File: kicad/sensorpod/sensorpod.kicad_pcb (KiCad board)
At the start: 2 copper layers, 55.4 x 79.5 mm, 48 parts, among them M1 MOTOR, P1 HEADER_(8_WAY), Q1 IRFML8244TRPBF

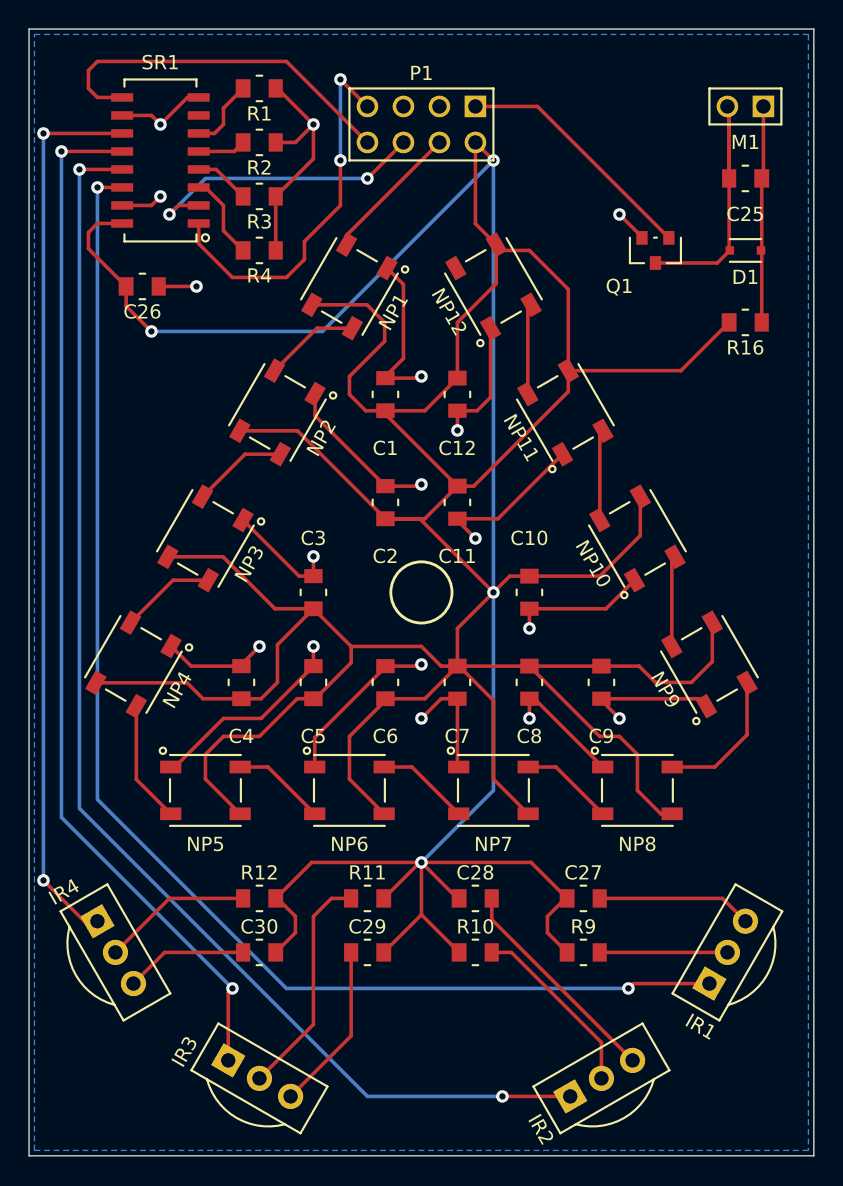
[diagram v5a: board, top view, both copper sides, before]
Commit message: Updated sensorpod schematic and PCB to fit into Serpac C9 enclosure
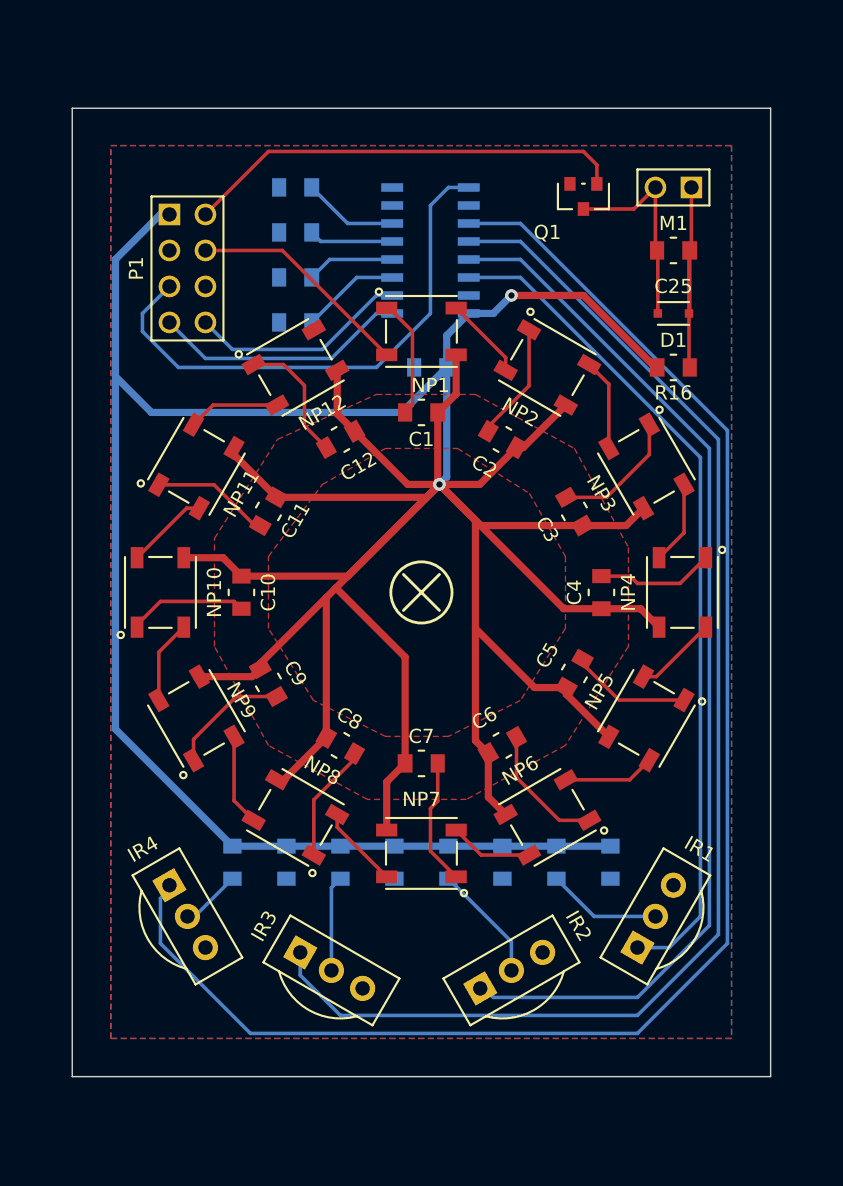
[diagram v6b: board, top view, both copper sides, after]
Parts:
- C26, C27, C28, C29, C30, R1, R10, R11, R12, R2, R3, R4, R9, SR1: moved to B.Cu
- moved NP4 39.1 mm to (216.5, 176.5), turned to 90 degrees
- moved NP9 36.4 mm to (182.2, 185.4)
- moved NP10 33.9 mm to (179.7, 176.5), turned to 270 degrees
- moved NP3 31.5 mm to (214.0, 167.6), turned to 120 degrees
- moved NP5 31.5 mm to (214.0, 185.4), turned to 60 degrees
- moved NP11 26.3 mm to (182.2, 167.6), turned to 240 degrees
- moved C4 26.2 mm to (210.8, 176.5)
- moved C30 25.6 mm to (211.5, 195.6), turned to 270 degrees
- moved NP8 24.2 mm to (189.2, 192.4), turned to 330 degrees
- moved C9 23.5 mm to (187.3, 182.9), turned to 300 degrees
- moved C27 21.1 mm to (188.6, 195.6), turned to 270 degrees
- moved C26 21.1 mm to (198.8, 160.7), turned to 180 degrees
- moved C10 20.3 mm to (185.4, 176.5)
- moved SR1 20.1 mm to (198.8, 152.4)
- moved P1 19.4 mm to (181.6, 153.7), turned to 270 degrees
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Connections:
- P1 pad 1: N-0000020 (its old number) -> +5V
- P1 pad 2: +5V -> N-0000021
- P1 pad 5: GND -> N-0000022
- P1 pad 6: N-0000018 (its old number) -> GND
- P1 pad 8: N-0000022 -> N-0000023
- Q1 pad 1: N-0000020 (its old number) -> N-0000021
- SR1 pad 2: N-0000018 (its old number) -> N-0000023
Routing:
- net GND: track 198.4 -> 104.0 mm, vias 17 -> 0
- net +5V: track 408.0 -> 333.2 mm, vias 4 -> 2
- net N-0000027: track 63.3 -> 110.1 mm, vias 2 -> 0
- net N-000002: track 93.8 -> 59.4 mm, vias 2 -> 0
- net N-0000021: track 0.00 -> 31.2 mm
- net N-0000018 (its old number): track 20.9 -> 0.00 mm, vias 2 -> 0
- net N-0000011: track 73.5 -> 93.0 mm, vias 2 -> 0
- net N-0000020 (its old number): track 17.5 -> 0.00 mm
- net N-000001: track 91.1 -> 74.7 mm, vias 2 -> 0
- net N-0000023: track 0.00 -> 15.5 mm
- net N-0000022: track 26.2 -> 37.8 mm
- net N-0000032: track 16.2 -> 6.73 mm
- net N-0000024: track 26.8 -> 18.1 mm, vias 2 -> 0
- net N-0000034: track 10.6 -> 4.28 mm
- net N-0000020: track 20.8 -> 14.7 mm
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- added copper zone on F.Cu, net +5V
- added copper zone on F.Cu, net GND
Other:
- board size 55.4 x 79.5 mm -> 49.3 x 68.3 mm
- net class +5V added: clearance 0.508, trace_width 0.508, via_dia 0.889, via_drill 0.635

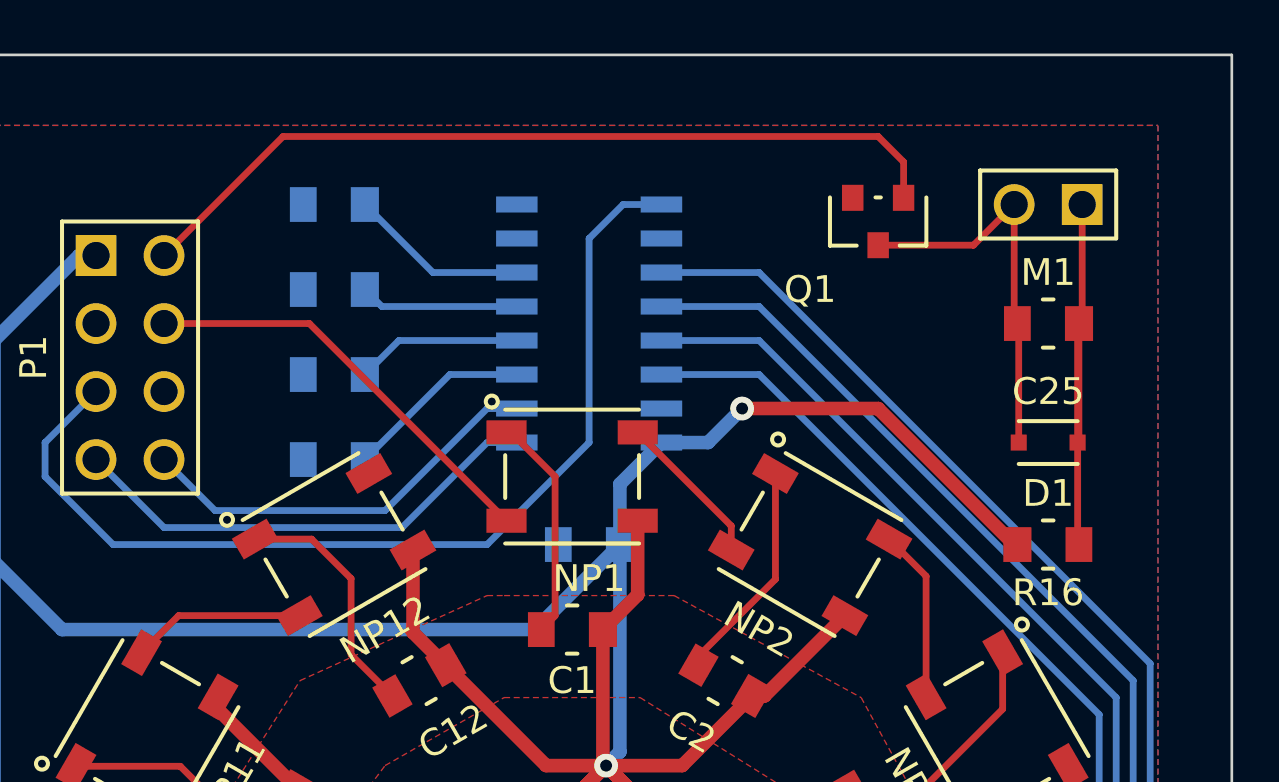
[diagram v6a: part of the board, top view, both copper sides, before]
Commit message: Remove vibration motor from sensor pos - it will just be in the command pod
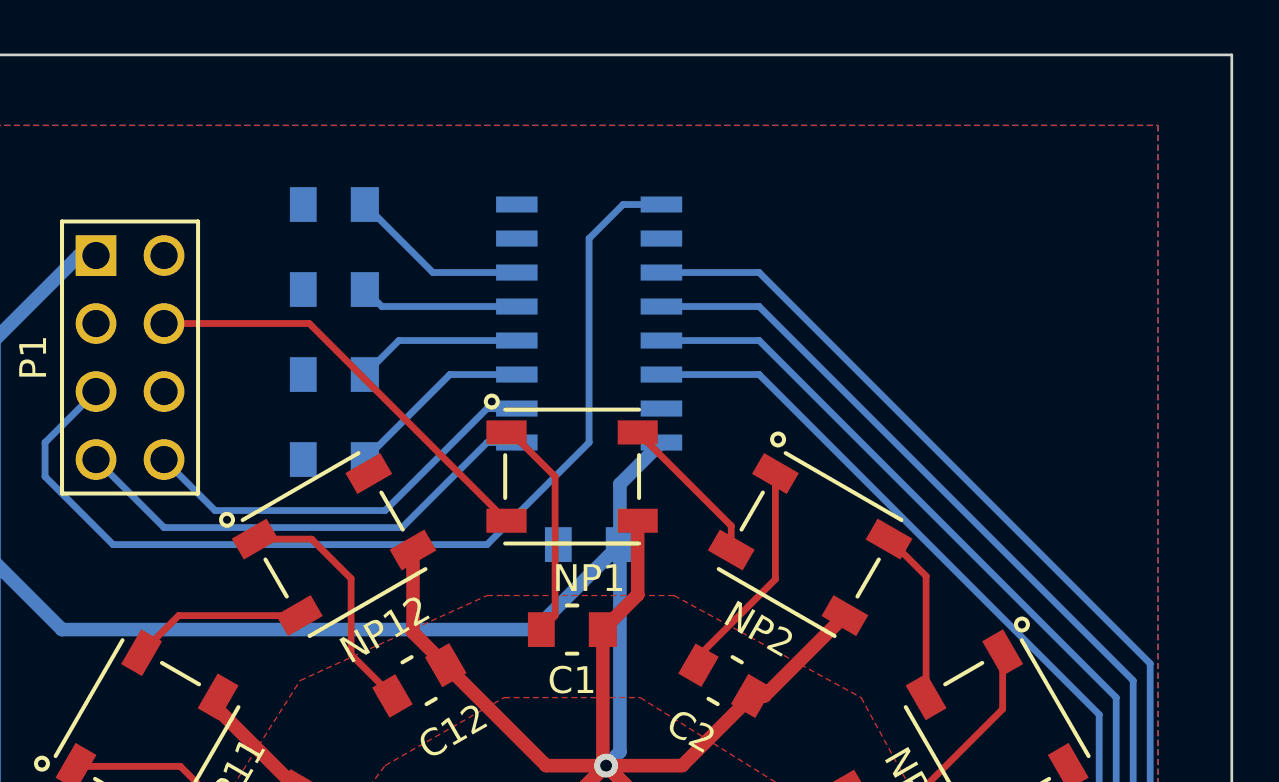
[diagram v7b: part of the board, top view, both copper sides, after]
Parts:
- removed C25: GENERIC_CAPACITOR, 0805
- removed D1: GENERIC_DIODE, SOD-323
- removed M1: MOTOR, Header_2x1
- removed Q1: IRFML8244TRPBF, SOT-23
- removed R16: GENERIC_RESISTOR, 0805
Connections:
- P1 pad 2: N-0000021 -> (no net)
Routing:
- net N-0000021: track 31.2 -> 0.00 mm
- net N-000009 (its old number): track 17.3 -> 0.00 mm
- net +5V: track 333.2 -> 317.3 mm, vias 2 -> 1
- net N-0000020: track 14.7 -> 0.00 mm

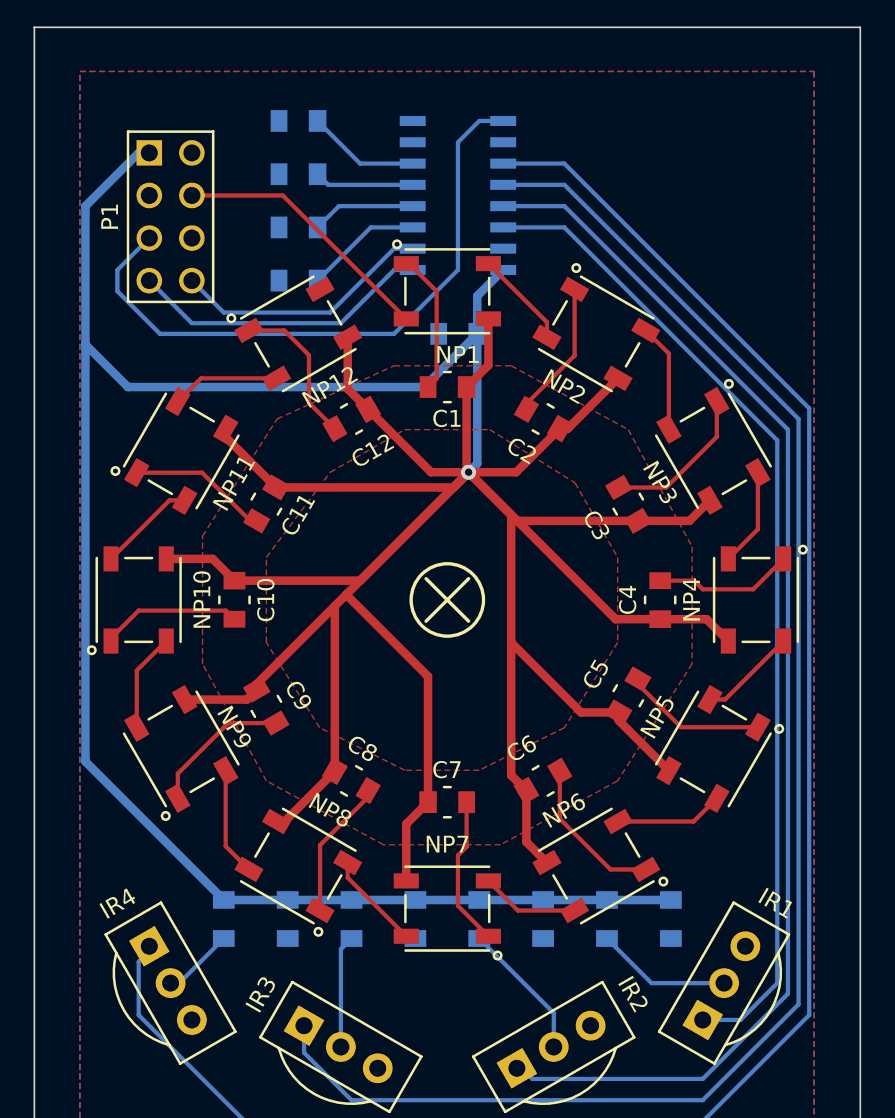
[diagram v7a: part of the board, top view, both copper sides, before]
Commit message: Moved shift register to allow more room for cable entry
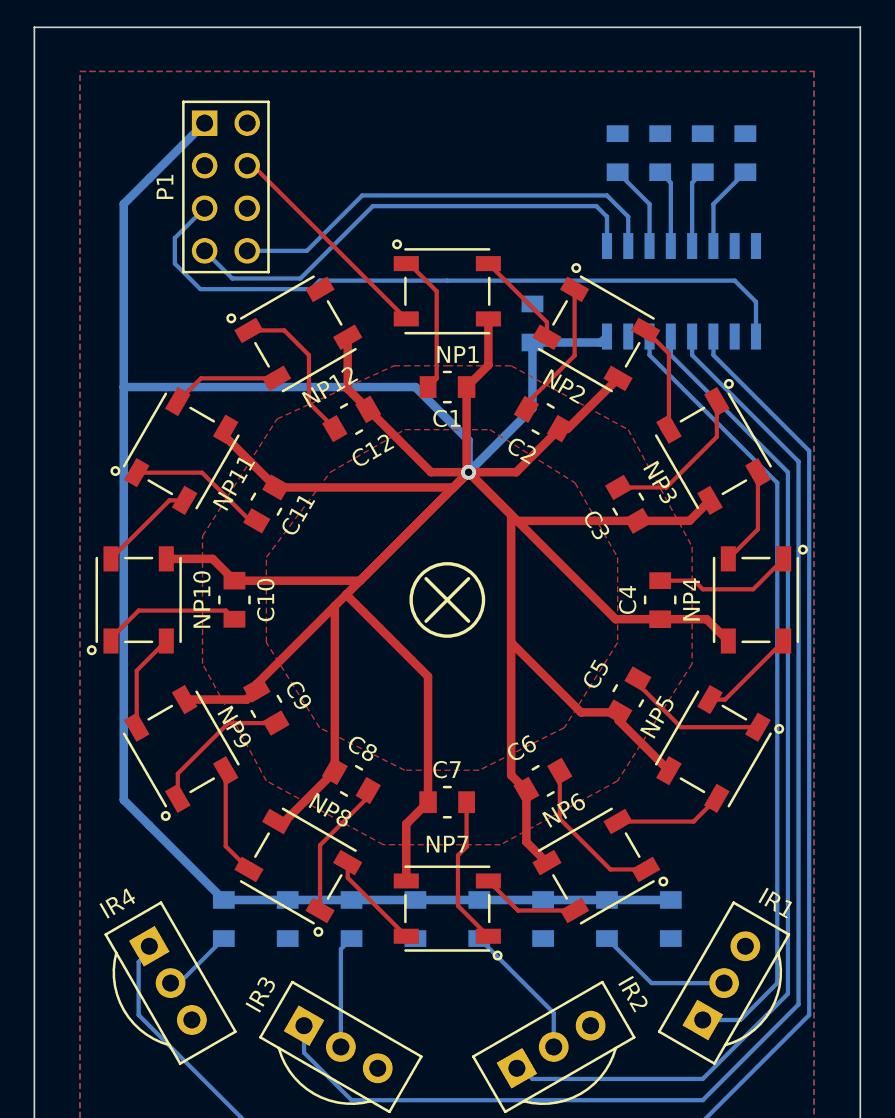
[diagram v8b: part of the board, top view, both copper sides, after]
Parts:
- moved R1 26.7 mm to (215.9, 149.9), turned to 90 degrees
- moved R2 24.2 mm to (213.4, 149.9), turned to 90 degrees
- moved R3 22.0 mm to (210.8, 149.9), turned to 90 degrees
- moved R4 20.5 mm to (208.3, 149.9), turned to 90 degrees
- moved SR1 14.5 mm to (212.1, 158.1), turned to 0 degrees
- moved C26 4.49 mm to (203.2, 160.0), turned to 90 degrees
- moved P1 3.75 mm to (184.9, 151.9)
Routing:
- net N-0000024: track 110.1 -> 92.5 mm
- net N-0000025: track 93.0 -> 77.1 mm
- net N-0000026: track 74.7 -> 60.6 mm
- net N-0000027: track 59.4 -> 47.1 mm
- net N-0000023: track 15.5 -> 26.4 mm
- net N-0000018: track 18.1 -> 28.5 mm
- net N-0000017: track 37.8 -> 42.1 mm
- net N-0000022: track 15.8 -> 13.3 mm
- net N-0000013: track 6.99 -> 5.19 mm
- net N-0000016: track 6.73 -> 5.19 mm
- net N-0000014: track 6.20 -> 4.67 mm
- net N-0000015: track 5.94 -> 4.67 mm
